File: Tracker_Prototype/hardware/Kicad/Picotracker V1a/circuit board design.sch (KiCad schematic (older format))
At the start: 34 parts, among them J1 Conn_01x06, J2 GND, J3 3.3V, J4 Unconnected, SW1 SW_Push, U1 MAX-M8C, U3 CMWX1ZZABZ-078, U6 MS5607-02BA

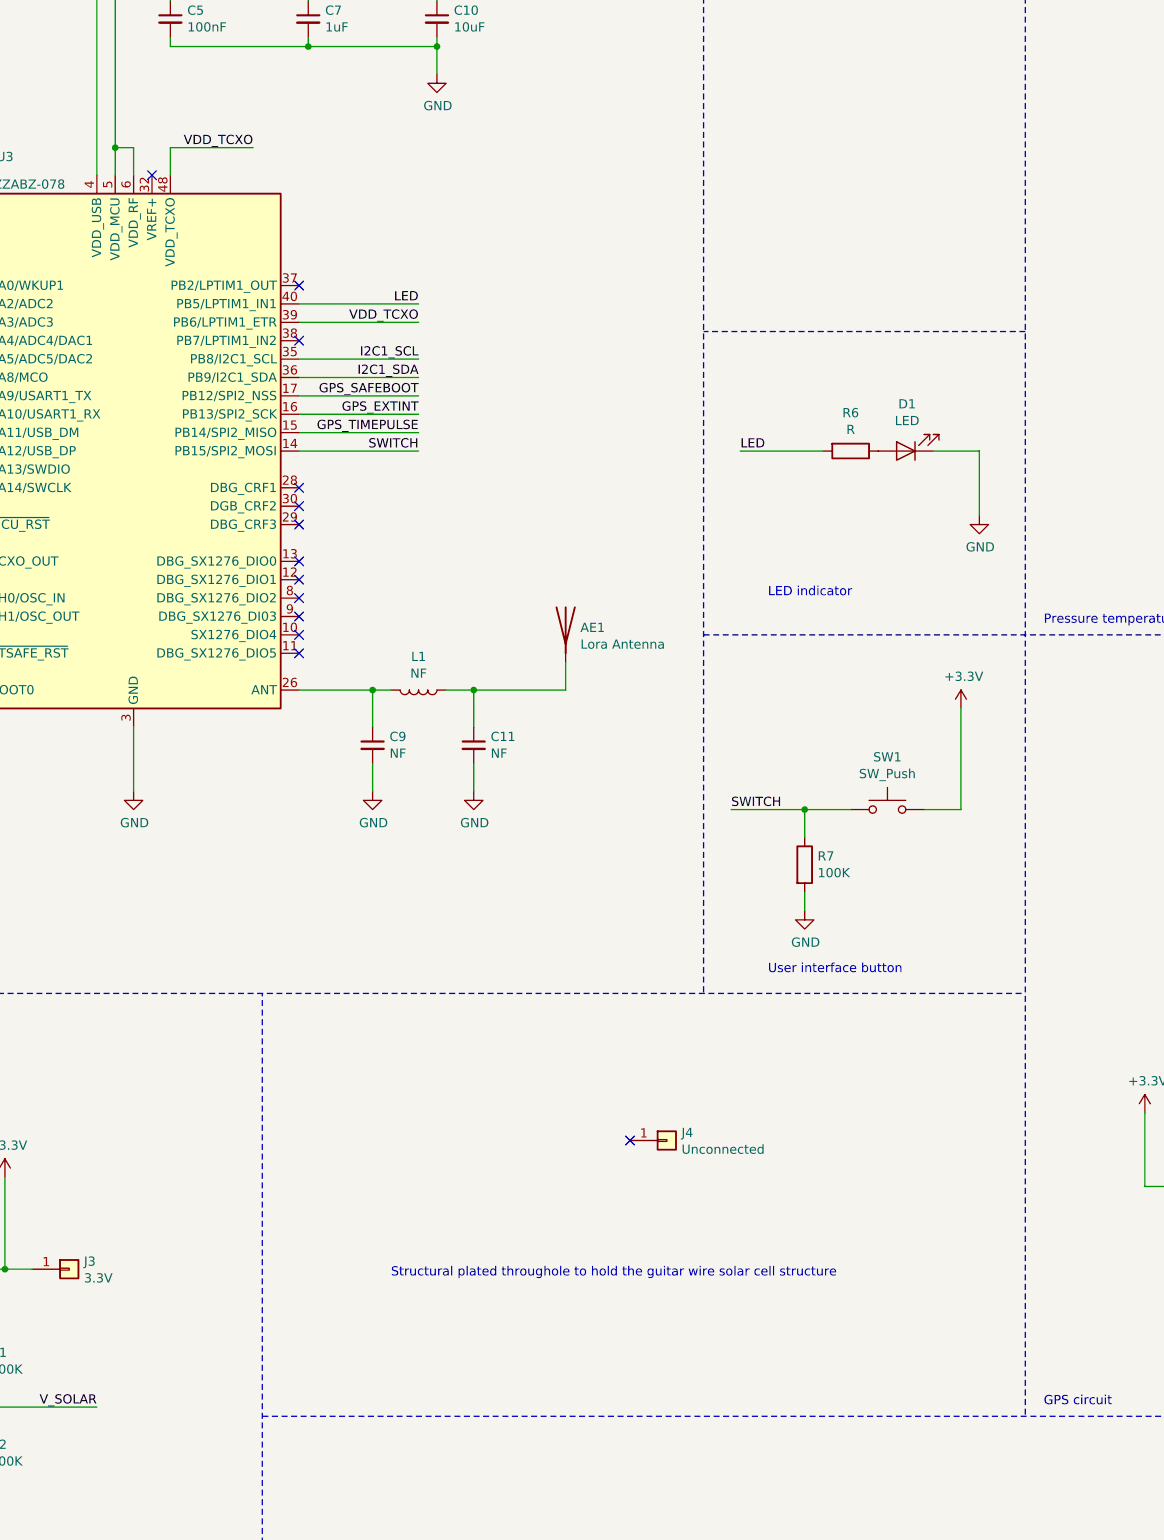
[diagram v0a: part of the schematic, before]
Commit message: added the switch. reorganised the prototype folder to have a "a" variant
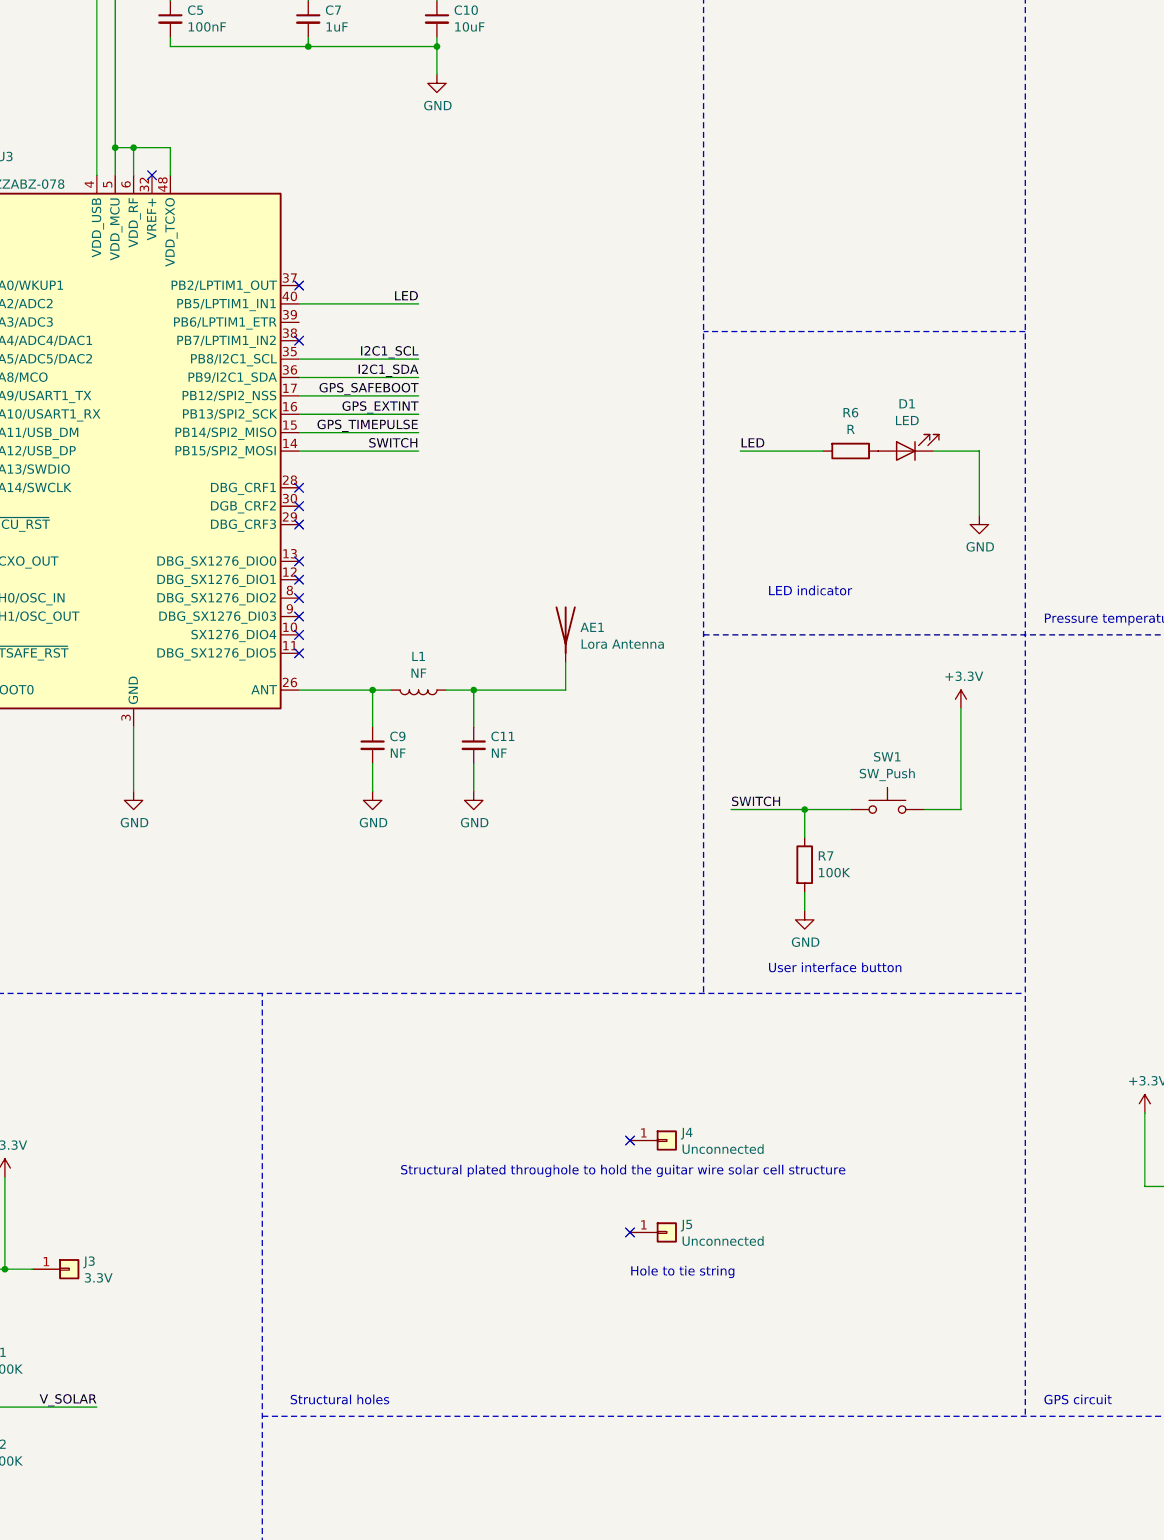
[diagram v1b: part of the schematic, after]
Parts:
- added J5: Unconnected, Connector_Wire:SolderWirePad_1x01_Drill0.8mm, symbol Connector_Generic:Conn_01x01
- SW1: footprint (none) -> flight-computer:EVPAWCD4A
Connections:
- net +3V3: now also U3.48 (VDD_TCXO)
- net VDD_TCXO: no longer names the net of U3.39 (PB6/LPTIM1_ETR)
- net VDD_TCXO: no longer U3.48 (VDD_TCXO)
- no-connect marks 31 -> 32
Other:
- note added: "Hole to tie string\n"
- note added: "Structural holes\n"
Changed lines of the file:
@@
 Connection ~ 7900 1700
-Wire Wire Line
-	6450 2250 6900 2250
-Text Label 6900 2250 2    50   ~ 0
-VDD_TCXO
 Wire Wire Line
 	7550 5200 7550 5400
@@
 Text Label 4900 4000 0    50   ~ 0
 SWDIO
-Text Label 7800 3200 2    50   ~ 0
-VDD_TCXO
-Wire Wire Line
-	7150 3200 7800 3200
 Wire Wire Line
 	6050 1350 6050 2400
@@
 Wire Notes Line
 	6950 9150 16050 9150
-Text Notes 7650 8400 0    50   ~ 0
+Text Notes 7700 7850 0    50   ~ 0
 Structural plated throughole to hold the guitar wire solar cell structure
 Wire Wire Line
@@
 F 0 "SW1" H 10350 6135 50  0000 C CNN
 F 1 "SW_Push" H 10350 6044 50  0000 C CNN
-F 2 "" H 10350 6050 50  0001 C CNN
+F 2 "flight-computer:EVPAWCD4A" H 10350 6050 50  0001 C CNN
 F 3 "~" H 10350 6050 50  0001 C CNN
 	1    10350 5850
@@
 Text Notes 9700 4700 0    50   ~ 0
 LED indicator\n
+$Comp
+L Connector_Generic:Conn_01x01 J5
+U 1 1 5DB85E84
+P 9150 8150
+F 0 "J5" H 9230 8192 50  0000 L CNN
+F 1 "Unconnected" H 9230 8101 50  0000 L CNN
+F 2 "Connector_Wire:SolderWirePad_1x01_Drill0.8mm" H 9150 8150 50  0001 C CNN
+F 3 "~" H 9150 8150 50  0001 C CNN
+	1    9150 8150
+	1    0    0    -1
+$EndComp
+NoConn ~ 8950 8150
+Text Notes 8950 8400 0    50   ~ 0
+Hole to tie string\n
+Text Notes 7100 9100 0    50   ~ 0
+Structural holes\n
+Wire Wire Line
+	6450 2250 6250 2250
+Connection ~ 6250 2250
 $EndSCHEMATC

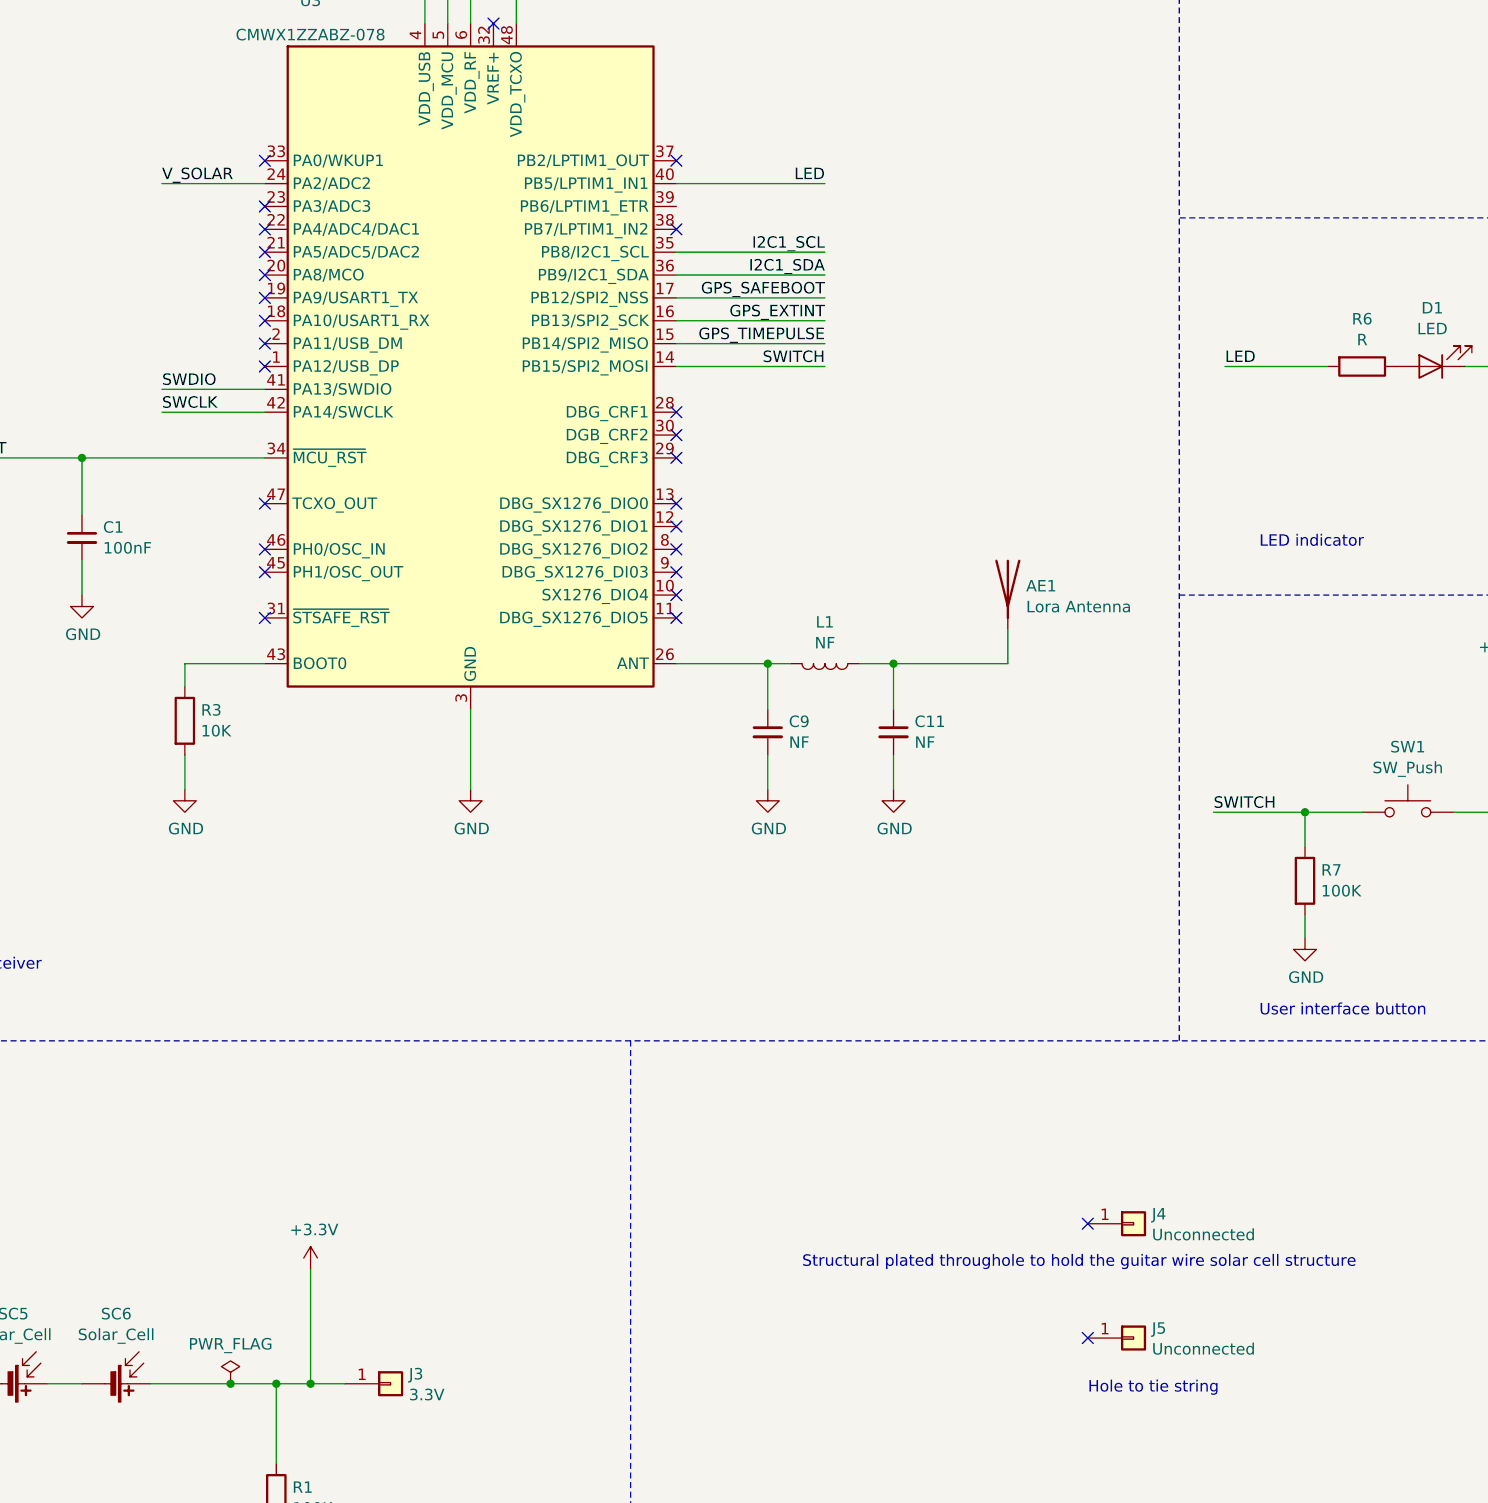
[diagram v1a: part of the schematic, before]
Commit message: finished the layout of the simple version a
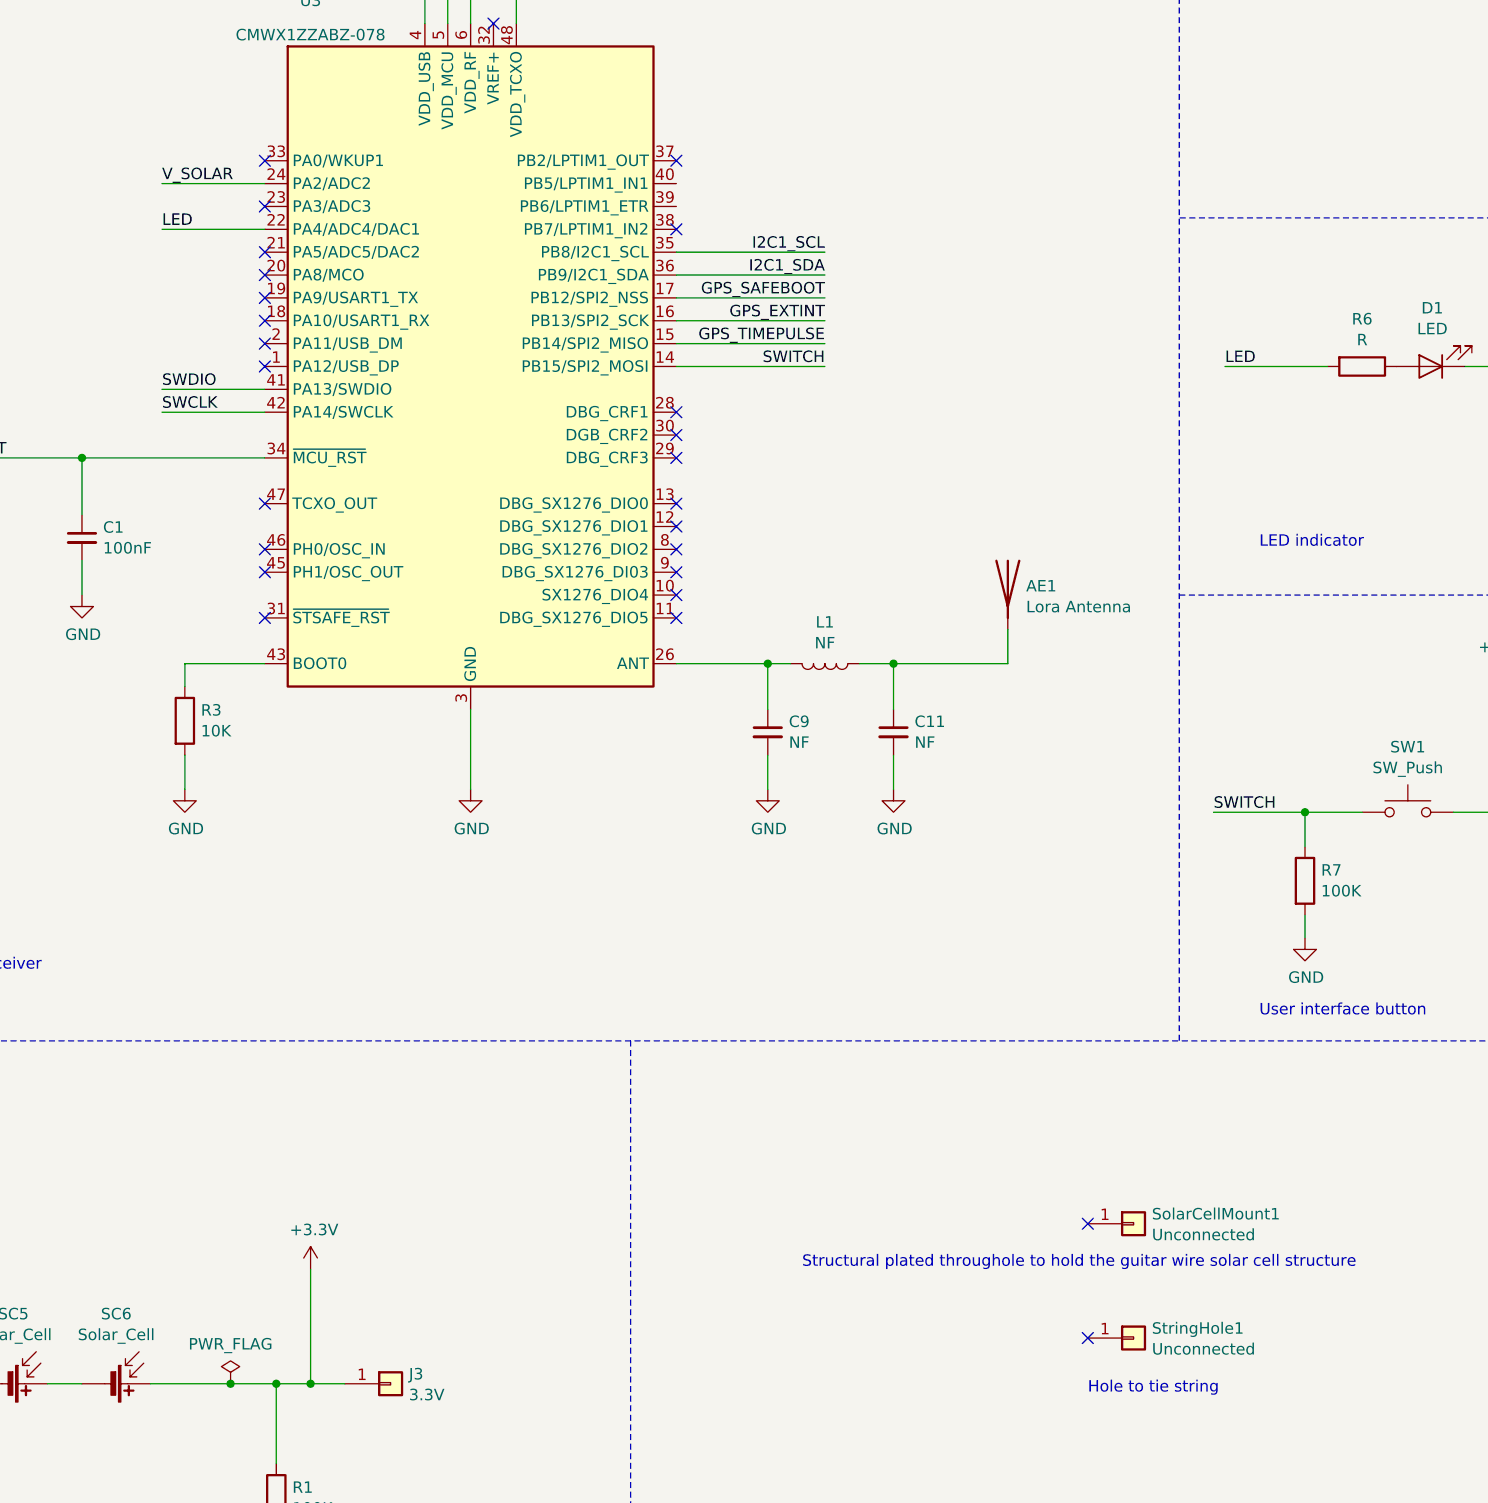
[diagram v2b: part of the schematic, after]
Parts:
- StringHole1: renamed from J5; footprint Connector_Wire:SolderWirePad_1x01_Drill0.8mm -> flight-computer:SolderWirePad_1x01_Drill0.8mm
- renumbered J4 to SolarCellMount1
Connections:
- net LED: now also U3.22 (PA4/ADC4/DAC1); no longer U3.40 (PB5/LPTIM1_IN1)
- no-connect marks 32 -> 31
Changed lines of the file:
@@
 NoConn ~ 5350 3500
 NoConn ~ 5350 3400
-NoConn ~ 5350 3300
 NoConn ~ 5350 3200
 NoConn ~ 5350 3000
@@
 	1250 8350 1450 8350
 $Comp
-L Connector_Generic:Conn_01x01 J4
+L Connector_Generic:Conn_01x01 SolarCellMount1
 U 1 1 5DCBAB7A
 P 9150 7650
-F 0 "J4" H 9230 7692 50  0000 L CNN
+F 0 "SolarCellMount1" H 9230 7692 50  0000 L CNN
 F 1 "Unconnected" H 9230 7601 50  0000 L CNN
 F 2 "Connector_Wire:SolderWirePad_1x01_Drill0.8mm" H 9150 7650 50  0001 C CNN
@@
 NoConn ~ 5350 3900
 Wire Wire Line
-	7150 3100 7800 3100
+	5350 3300 4900 3300
 Wire Wire Line
 	10850 3900 10850 4250
@@
 Wire Notes Line
 	9350 650  9350 6850
-Text Label 7800 3100 2    50   ~ 0
+Text Label 4900 3300 0    50   ~ 0
 LED
 Text Label 9550 3900 0    50   ~ 0
@@
 LED indicator\n
 $Comp
-L Connector_Generic:Conn_01x01 J5
+L Connector_Generic:Conn_01x01 StringHole1
 U 1 1 5DB85E84
 P 9150 8150
-F 0 "J5" H 9230 8192 50  0000 L CNN
+F 0 "StringHole1" H 9230 8192 50  0000 L CNN
 F 1 "Unconnected" H 9230 8101 50  0000 L CNN
-F 2 "Connector_Wire:SolderWirePad_1x01_Drill0.8mm" H 9150 8150 50  0001 C CNN
+F 2 "flight-computer:SolderWirePad_1x01_Drill0.8mm" H 9150 8150 50  0001 C CNN
 F 3 "~" H 9150 8150 50  0001 C CNN
 	1    9150 8150

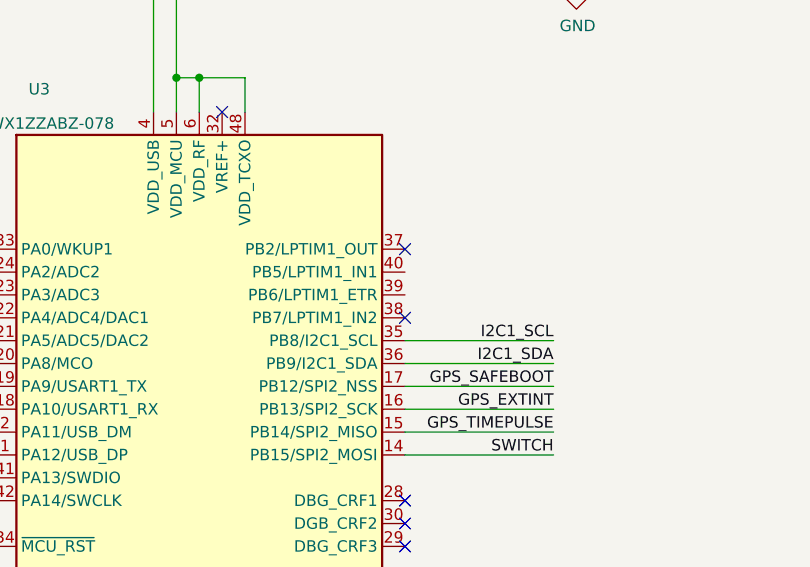
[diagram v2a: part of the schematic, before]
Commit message: mostly wired up the "b" variant. Changed the fill clearance for copper pour for the "a" variant to a much smaller 0.15mm
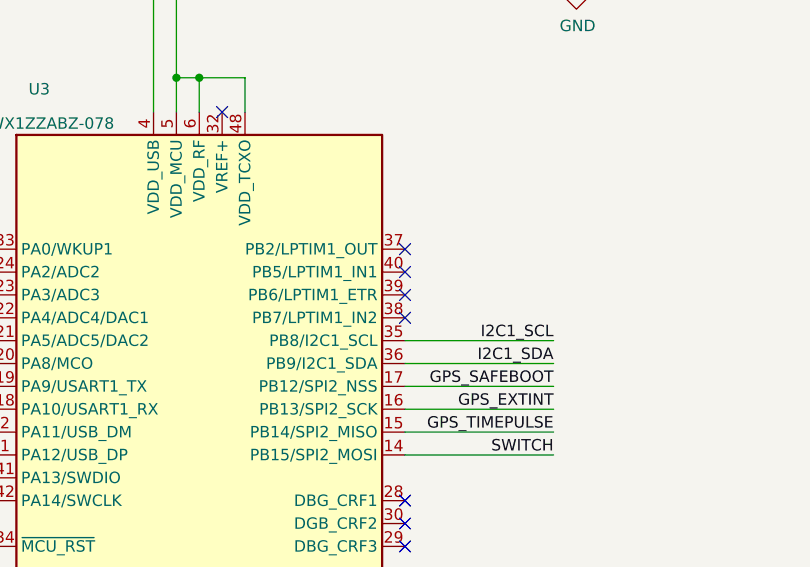
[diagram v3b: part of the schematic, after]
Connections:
- no-connect marks 31 -> 33
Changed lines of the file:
@@
 	6450 2250 6250 2250
 Connection ~ 6250 2250
+NoConn ~ 7150 3100
+NoConn ~ 7150 3200
 $EndSCHEMATC
